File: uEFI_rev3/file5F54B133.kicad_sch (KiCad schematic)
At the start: 36 parts, among them U10 SensorsV2, U11 SensorsV2, U12 SensorsV2, U13 SensorsV2, U14 SensorsV2, U2 SensorsV2, U27 LM321, U31 LM321, U8 SensorsV2, U9 SensorsV2

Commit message: rev3, analog inputs
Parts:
- removed D14, D18: DZ2S033X0L, Diode_SMD:D_MiniMELF, symbol Diode:DZ2S033X0L
- removed JP11, JP19: Jumper_NC_Small, Jumper:SolderJumper-2_P1.3mm_Open_TrianglePad1.0x1.5mm, symbol Device:Jumper_NC_Small
- removed TP10, TP11, TP12, TP13, TP14, TP15, TP16, TP17: TestPoint, TestPoint:TestPoint_Pad_2.0x2.0mm, symbol Connector:TestPoint
- removed U10, U11, U12, U13, U14, U2, U8, U9: SensorsV2, OpenEFI-STM32F_rev3:Sensors_v2, symbol OpenEFI-STM32-rev3:SensorsV2
- added C1, C32, C35, C37, C38, C4: 240pF, Capacitor_SMD:C_0603_1608Metric, symbol Device:C_Small
- added C39: 100nF, Capacitor_SMD:C_0805_2012Metric, symbol Device:C_Small
- added C40: 4.7uF, Capacitor_SMD:C_0805_2012Metric, symbol Device:CP_Small
- added D15, D16, D17, D18, D19, D20, D21, D22, D23, D24, D25, D26, D27, D28, D29, D30: K26, Diode_SMD:D_SOD-123F, symbol Diode:PMEG2020EH
- added JP10, JP12, JP5, JP6, JP7, JP8, JP9: Jumper_NC_Small, Jumper:SolderJumper-2_P1.3mm_Open_TrianglePad1.0x1.5mm, symbol Device:Jumper_NC_Small
- added R36, R37, R42, R43, R49, R50: 28.6k +-1%, Resistor_SMD:R_0603_1608Metric, symbol Device:R_Small
- added R38, R39, R44, R45, R51, R52: 2.2k, Resistor_SMD:R_0603_1608Metric, symbol Device:R_Small
- added R40, R41, R47, R48, R53, R54: 3.32k +-1%, Resistor_SMD:R_0603_1608Metric, symbol Device:R_Small
- added R46: 0, Resistor_SMD:R_0603_1608Metric, symbol Device:R_Small
- added R55: 10k, Resistor_SMD:R_0603_1608Metric, symbol Device:R_Small
- added RV1: 2k, Potentiometer_THT:Potentiometer_Bourns_3386C_Horizontal, symbol Device:R_Potentiometer
- added U2: MCP3208, Package_SO:SOIC-16_3.9x9.9mm_P1.27mm, symbol Analog_ADC:MCP3208
- added U8: LM4040DBZ-5, Package_TO_SOT_SMD:SOT-23, symbol Reference_Voltage:LM4040DBZ-5
- added U9: AMS1117-5.0, Package_TO_SOT_SMD:SOT-223-3_TabPin2, symbol Regulator_Linear:AMS1117-5.0
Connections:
- net +12V: now also R55.2, U9.3 (VI)
- net B1: now also C1.1, R36.1, R38.2, R40.1; no longer C49.1, R87.1, R92.1, R97.2
- net C1: now also C4.1, R37.1, R39.2, R41.1
- net D1: now also C32.1, R42.1, R44.2, R47.1
- net E1: now also C35.1, R43.1, R45.2, R48.1
- net F1: now also C37.1, R49.1, R51.2, R53.1
- net G1: now also C38.1, R50.1, R52.2, R54.1
- net GND: now also R46.2, U2.9 (DGND); no longer C49.2, C51.2, R109.1, R83.2, R87.2, U27.2 (V-), U31.2 (V-)
- net K1: now also C49.1, R87.1, R92.1, R97.2
- net CH6: now reaches JP15.2, JP18.1, TP18.1, U31.4
- net CH6: now also D17.2 (A), D20.1 (K), U2.7 (CH6)
- net CH7: now reaches TP19.1, U27.3 (-), U27.4
- net CH7: now also D25.2 (A), D28.1 (K), JP12.1
- net +5V renamed +5C
- net +5C: now also C40.1, D15.1 (K), D16.1 (K), D17.1 (K), D21.1 (K), D22.1 (K), D25.1 (K), D26.1 (K), D27.1 (K), R36.2, R37.2, R42.2, R49.2, R50.2, U2.16 (Vdd), U9.2 (VO)
- new net: JP9.2, U2.5 (CH4)
- new net: C39.1, RV1.1, U9.1 (GND)
- new net: JP8.2, U2.4 (CH3)
- new net: JP10.2, U2.6 (CH5)
- new net: JP5.2, U2.1 (CH0)
- new net: JP6.2, U2.2 (CH1)
- new net: JP7.2, U2.3 (CH2)
- new net: JP12.2, U2.8 (CH7)
- new net +5VL: R55.1, U2.15 (Vref), U8.1 (K)
- new net ADC_CS: U2.10 (~{CS}/SHDN)
- new net CH0: D16.2 (A), D19.1 (K), JP5.1, R38.1
- new net CH1: D15.2 (A), D18.1 (K), JP6.1, R39.1
- new net CH2: D21.2 (A), D23.1 (K), JP7.1, R44.1
- new net CH3: D22.2 (A), D24.1 (K), JP8.1, R45.1
- new net CH4: D26.2 (A), D29.1 (K), JP9.1, R51.1
- new net CH5: D27.2 (A), D30.1 (K), JP10.1, R52.1
- new net GNDA: C1.2, C32.2, C35.2, C37.2, C38.2, C39.2, C4.2, C40.2, C49.2, C51.2, D18.2 (A), D19.2 (A), D20.2 (A), D23.2 (A), D24.2 (A), D28.2 (A), D29.2 (A), D30.2 (A), R109.1, R40.2, R41.2, R46.1, R47.2, R48.2, R53.2, R54.2, R83.2, R87.2, RV1.2, U2.14 (AGND), U27.2 (V-), U31.2 (V-), U8.2 (A)
- new net SPI2_MISO: U2.12 (Dout)
- new net SPI2_MOSI: U2.11 (Din)
- new net SPI2_SCK: U2.13 (CLK)
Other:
- note added: "0"
- note added: "1"
- note added: "2"
- note added: "3"
- note added: "4"
- note added: "5"
- note added: "5.5V"
- note added: "5v ADC Vref"
- note added: "5v ref: AnaSem VRH5501NTX LCSC C698020"
- note added: "ADC"
- note added: "AGND Star"
- note added: "Sensores: Temp Aire Temp Refrigerante TPS MAP O2 Bateria"
- note added: "Solo en puentear si no se utiliza una wideband"
- note removed: "AIR_TEMP"
- note removed: "PRES_FUEL"
- note removed: "PRES_OIL"
- note removed: "Solo en puentear si no te utiliza una wideband"
- note removed: "TEMP"
- note removed: "TPS"
- moved on the sheet: C49, C51, JP15, JP17, JP18, R108, R109, R82, R83, R87, R92, R97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

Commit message: rev3 ADC SPI
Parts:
- removed RV1: 2k, Potentiometer_THT:Potentiometer_Bourns_3386C_Horizontal, symbol Device:R_Potentiometer
- removed U9: AMS1117-5.0, Package_TO_SOT_SMD:SOT-223-3_TabPin2, symbol Regulator_Linear:AMS1117-5.0
- added R56: 750, Resistor_SMD:R_0603_1608Metric, symbol Device:R_Small
- added R57: 220, Resistor_SMD:R_0603_1608Metric, symbol Device:R_Small
- added U10, U11: TXS0102DCU, Package_SO:VSSOP-8_2.3x2mm_P0.5mm, symbol Logic_LevelTranslator:TXS0102DCU
- added U9: AMS1117, Package_TO_SOT_SMD:SOT-223-3_TabPin2, symbol Regulator_Linear:AMS1117
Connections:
- net +12V: now also U9.3 (VI)
- net +5C: now also R56.1, U9.2 (VO)
- net ADC_CS: now also U11.4 (A2); no longer U2.10 (~{CS}/SHDN)
- net GND: now also U10.2 (GND), U11.2 (GND)
- net GNDA: now also R57.1
- net SPI2_MISO: now also U10.4 (A2); no longer U2.12 (Dout)
- net SPI2_MOSI: now also U11.5 (A1); no longer U2.11 (Din)
- net SPI2_SCK: now also U10.5 (A1); no longer U2.13 (CLK)
- net at C39.1: now also R56.2, R57.2, U9.1 (ADJ)
- new net +3V3: U10.3 (VCCA), U10.6 (OE), U11.3 (VCCA), U11.6 (OE)
- new net +5V: U10.7 (VCCB), U11.7 (VCCB)
- new net CLK: U10.8 (B1), U2.13 (CLK)
- new net CS: U11.1 (B2), U2.10 (~{CS}/SHDN)
- new net DIN: U11.8 (B1), U2.11 (Din)
- new net DOUT: U10.1 (B2), U2.12 (Dout)
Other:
- note added: "SPI 5V => 3V"

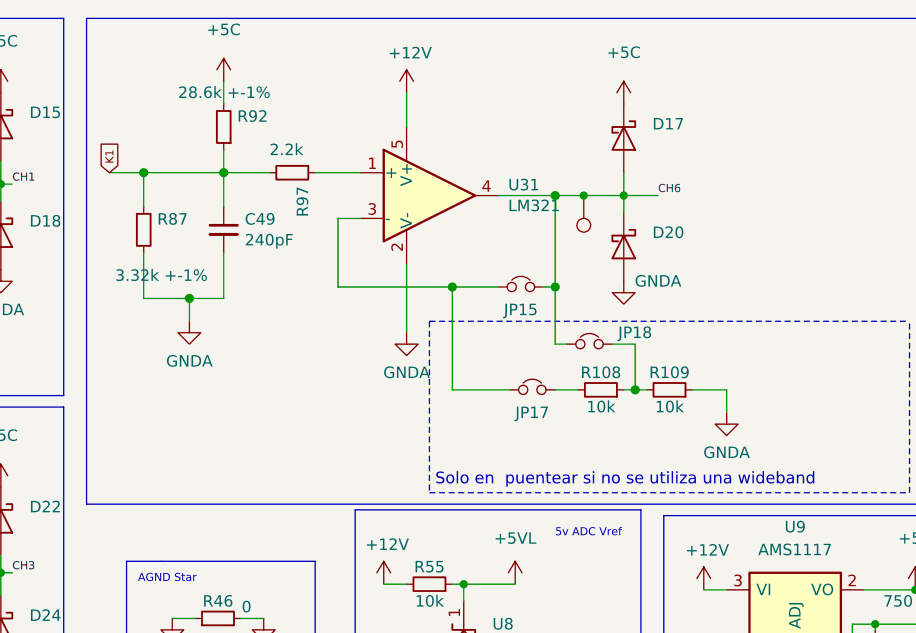
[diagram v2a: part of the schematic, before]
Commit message: rev3, PMIC, Relays done
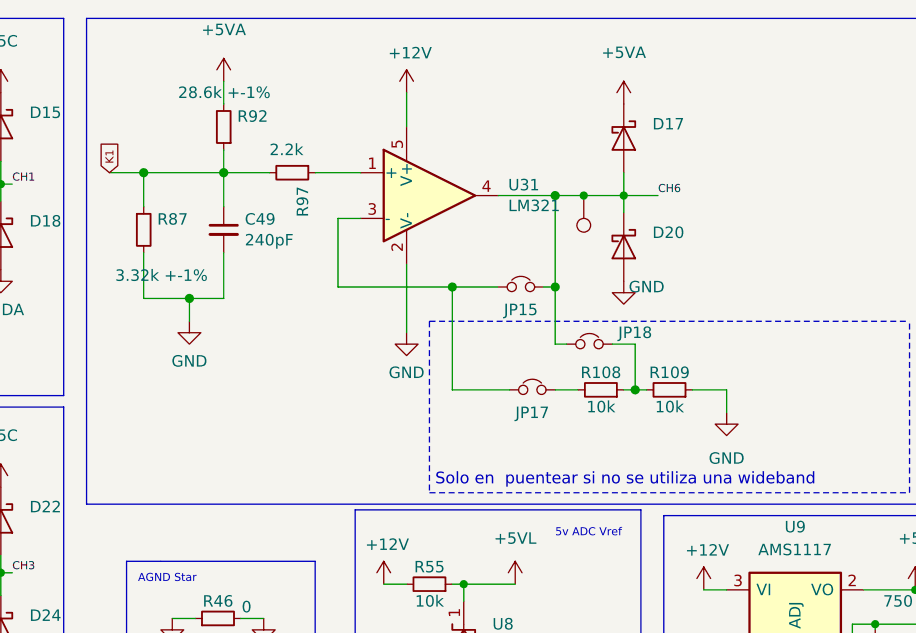
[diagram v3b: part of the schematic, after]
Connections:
- net +5C: no longer D17.1 (K), R92.2
- net GND: now also C49.2, D20.2 (A), R109.1, R87.2, U31.2 (V-)
- net GNDA: no longer C49.2, D20.2 (A), R109.1, R87.2, U31.2 (V-)
- new net +5VA: D17.1 (K), R92.2
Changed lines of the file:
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@@
   (symbol (lib_id "power:+5V") (at 283.21 222.25 0) (unit 1)
     (in_bom yes) (on_board yes) (fields_autoplaced)
-    (property "Reference" "#PWR?" (id 0) (at 283.21 226.06 0)
+    (property "Reference" "#PWR0138" (id 0) (at 283.21 226.06 0)
       (effects (font (size 1.27 1.27)) hide)
     )
@@
     (pin "2")
   )
+  (symbol (lib_id "power:GND") (at 176.53 118.11 0) (unit 1)
+    (in_bom yes) (on_board yes)
+    (property "Reference" "#PWR?" (id 0) (at 176.53 124.46 0)
+      (effects (font (size 1.27 1.27)) hide)
+    )
+    (property "Value" "GND" (id 1) (at 176.53 122.555 0))
+    (property "Footprint" "" (id 2) (at 176.53 118.11 0)
+      (effects (font (size 1.27 1.27)) hide)
+    )
+    (property "Datasheet" "" (id 3) (at 176.53 118.11 0)
+      (effects (font (size 1.27 1.27)) hide)
+    )
+    (pin "1")
+  )
   (symbol (lib_id "Diode:PMEG2020EH") (at 224.79 109.855 270) (unit 1)
     (in_bom yes) (on_board yes) (fields_autoplaced)
@@
     (pin "1")
     (pin "2")
-  )
-  (symbol (lib_id "power:+5C") (at 224.79 93.98 0) (unit 1)
-    (in_bom yes) (on_board yes) (fields_autoplaced)
-    (property "Reference" "#PWR076" (id 0) (at 224.79 97.79 0)
-      (effects (font (size 1.27 1.27)) hide)
-    )
-    (property "Value" "+5C" (id 1) (at 224.79 88.265 0))
-    (property "Footprint" "" (id 2) (at 224.79 93.98 0)
-      (effects (font (size 1.27 1.27)) hide)
-    )
-    (property "Datasheet" "" (id 3) (at 224.79 93.98 0)
-      (effects (font (size 1.27 1.27)) hide)
-    )
-    (pin "1")
   )
   (symbol (lib_id "Device:Jumper_NC_Small") (at 241.3 186.055 0) (unit 1)
@@
     (pin "2")
   )
-  (symbol (lib_id "power:+5C") (at 180.34 91.44 0) (unit 1)
-    (in_bom yes) (on_board yes) (fields_autoplaced)
-    (property "Reference" "#PWR070" (id 0) (at 180.34 95.25 0)
-      (effects (font (size 1.27 1.27)) hide)
-    )
-    (property "Value" "+5C" (id 1) (at 180.34 85.725 0))
-    (property "Footprint" "" (id 2) (at 180.34 91.44 0)
-      (effects (font (size 1.27 1.27)) hide)
-    )
-    (property "Datasheet" "" (id 3) (at 180.34 91.44 0)
-      (effects (font (size 1.27 1.27)) hide)
-    )
-    (pin "1")
-  )
   (symbol (lib_id "Device:Jumper_NC_Small") (at 241.3 191.135 0) (unit 1)
     (in_bom yes) (on_board yes)
@@
     )
     (property "Datasheet" "" (id 3) (at 267.335 201.295 0)
-      (effects (font (size 1.27 1.27)) hide)
-    )
-    (pin "1")
-  )
-  (symbol (lib_id "power:GNDA") (at 176.53 118.11 0) (unit 1)
-    (in_bom yes) (on_board yes) (fields_autoplaced)
-    (property "Reference" "#PWR055" (id 0) (at 176.53 124.46 0)
-      (effects (font (size 1.27 1.27)) hide)
-    )
-    (property "Value" "GNDA" (id 1) (at 176.53 122.555 0))
-    (property "Footprint" "" (id 2) (at 176.53 118.11 0)
-      (effects (font (size 1.27 1.27)) hide)
-    )
-    (property "Datasheet" "" (id 3) (at 176.53 118.11 0)
       (effects (font (size 1.27 1.27)) hide)
     )
@@
     (pin "1")
   )
+  (symbol (lib_id "power:GND") (at 200.66 119.38 0) (unit 1)
+    (in_bom yes) (on_board yes)
+    (property "Reference" "#PWR?" (id 0) (at 200.66 125.73 0)
+      (effects (font (size 1.27 1.27)) hide)
+    )
+    (property "Value" "GND" (id 1) (at 200.66 123.825 0))
+    (property "Footprint" "" (id 2) (at 200.66 119.38 0)
+      (effects (font (size 1.27 1.27)) hide)
+    )
+    (property "Datasheet" "" (id 3) (at 200.66 119.38 0)
+      (effects (font (size 1.27 1.27)) hide)
+    )
+    (pin "1")
+  )
   (symbol (lib_id "power:+5C") (at 144.145 179.07 0) (unit 1)
     (in_bom yes) (on_board yes) (fields_autoplaced)
@@
     )
     (property "Datasheet" "" (id 3) (at 233.68 147.955 0)
-      (effects (font (size 1.27 1.27)) hide)
-    )
-    (pin "1")
-  )
-  (symbol (lib_id "power:GNDA") (at 224.79 113.665 0) (unit 1)
-    (in_bom yes) (on_board yes)
-    (property "Reference" "#PWR043" (id 0) (at 224.79 120.015 0)
-      (effects (font (size 1.27 1.27)) hide)
-    )
-    (property "Value" "GNDA" (id 1) (at 228.6 113.665 0))
-    (property "Footprint" "" (id 2) (at 224.79 113.665 0)
-      (effects (font (size 1.27 1.27)) hide)
-    )
-    (property "Datasheet" "" (id 3) (at 224.79 113.665 0)
       (effects (font (size 1.27 1.27)) hide)
     )
@@
     (pin "1")
   )
-  (symbol (lib_id "power:GNDA") (at 200.66 119.38 0) (unit 1)
-    (in_bom yes) (on_board yes) (fields_autoplaced)
-    (property "Reference" "#PWR058" (id 0) (at 200.66 125.73 0)
-      (effects (font (size 1.27 1.27)) hide)
-    )
-    (property "Value" "GNDA" (id 1) (at 200.66 123.825 0))
-    (property "Footprint" "" (id 2) (at 200.66 119.38 0)
-      (effects (font (size 1.27 1.27)) hide)
-    )
-    (property "Datasheet" "" (id 3) (at 200.66 119.38 0)
-      (effects (font (size 1.27 1.27)) hide)
-    )
-    (pin "1")
-  )
   (symbol (lib_id "power:+5C") (at 113.03 93.98 0) (unit 1)
     (in_bom yes) (on_board yes) (fields_autoplaced)
@@
     )
     (property "Datasheet" "" (id 3) (at 99.06 162.56 0)
-      (effects (font (size 1.27 1.27)) hide)
-    )
-    (pin "1")
-  )
-  (symbol (lib_id "power:GNDA") (at 236.22 128.27 0) (unit 1)
-    (in_bom yes) (on_board yes) (fields_autoplaced)
-    (property "Reference" "#PWR059" (id 0) (at 236.22 134.62 0)
-      (effects (font (size 1.27 1.27)) hide)
-    )
-    (property "Value" "GNDA" (id 1) (at 236.22 132.715 0))
-    (property "Footprint" "" (id 2) (at 236.22 128.27 0)
-      (effects (font (size 1.27 1.27)) hide)
-    )
-    (property "Datasheet" "" (id 3) (at 236.22 128.27 0)
       (effects (font (size 1.27 1.27)) hide)
     )
@@
     (pin "2")
   )
+  (symbol (lib_id "power:GND") (at 236.22 128.27 0) (unit 1)
+    (in_bom yes) (on_board yes) (fields_autoplaced)
+    (property "Reference" "#PWR?" (id 0) (at 236.22 134.62 0)
+      (effects (font (size 1.27 1.27)) hide)
+    )
+    (property "Value" "GND" (id 1) (at 236.22 133.35 0))
+    (property "Footprint" "" (id 2) (at 236.22 128.27 0)
+      (effects (font (size 1.27 1.27)) hide)
+    )
+    (property "Datasheet" "" (id 3) (at 236.22 128.27 0)
+      (effects (font (size 1.27 1.27)) hide)
+    )
+    (pin "1")
+  )
+  (symbol (lib_id "power:+5VA") (at 180.34 91.44 0) (unit 1)
+    (in_bom yes) (on_board yes) (fields_autoplaced)
+    (property "Reference" "#PWR0154" (id 0) (at 180.34 95.25 0)
+      (effects (font (size 1.27 1.27)) hide)
+    )
+    (property "Value" "+5VA" (id 1) (at 180.34 85.725 0))
+    (property "Footprint" "" (id 2) (at 180.34 91.44 0)
+      (effects (font (size 1.27 1.27)) hide)
+    )
+    (property "Datasheet" "" (id 3) (at 180.34 91.44 0)
+      (effects (font (size 1.27 1.27)) hide)
+    )
+    (pin "1")
+  )
   (symbol (lib_id "Device:R_Small") (at 151.765 189.23 270) (unit 1)
     (in_bom yes) (on_board yes)
@@
     )
     (property "Datasheet" "" (id 3) (at 155.575 112.395 0)
+      (effects (font (size 1.27 1.27)) hide)
+    )
+    (pin "1")
+  )
+  (symbol (lib_id "power:+5VA") (at 224.79 93.98 0) (unit 1)
+    (in_bom yes) (on_board yes) (fields_autoplaced)
+    (property "Reference" "#PWR0155" (id 0) (at 224.79 97.79 0)
+      (effects (font (size 1.27 1.27)) hide)
+    )
+    (property "Value" "+5VA" (id 1) (at 224.79 88.265 0))
+    (property "Footprint" "" (id 2) (at 224.79 93.98 0)
+      (effects (font (size 1.27 1.27)) hide)
+    )
+    (property "Datasheet" "" (id 3) (at 224.79 93.98 0)
       (effects (font (size 1.27 1.27)) hide)
     )
@@
       (effects (font (size 1.27 1.27)) hide)
     )
+    (pin "1")
+  )
+  (symbol (lib_id "power:GND") (at 224.79 113.665 0) (unit 1)
+    (in_bom yes) (on_board yes)
+    (property "Reference" "#PWR?" (id 0) (at 224.79 120.015 0)
+      (effects (font (size 1.27 1.27)) hide)
+    )
+    (property "Value" "GND" (id 1) (at 227.33 114.3 0))
+    (property "Footprint" "" (id 2) (at 224.79 113.665 0)
+      (effects (font (size 1.27 1.27)) hide)
+    )
+    (property "Datasheet" "" (id 3) (at 224.79 113.665 0)
+      (effects (font (size 1.27 1.27)) hide)
+    )

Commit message: uEFI rev 3.1.0
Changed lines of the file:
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@@
     (stroke (width 0) (type dash) (color 0 0 0 0))
   )
-  (polyline (pts (xy 123.825 84.455) (xy 162.56 84.455))
+  (polyline (pts (xy 123.825 84.455) (xy 163.83 84.455))
     (stroke (width 0) (type default) (color 0 0 0 0))
   )
@@
     (stroke (width 0) (type default) (color 0 0 0 0))
   )
-  (polyline (pts (xy 121.285 127.635) (xy 121.285 169.545))
+  (polyline (pts (xy 121.92 127.635) (xy 121.92 169.545))
     (stroke (width 0) (type default) (color 0 0 0 0))
   )
@@
     (stroke (width 0) (type solid) (color 0 0 0 0))
   )
-  (polyline (pts (xy 121.285 169.545) (xy 82.55 169.545))
+  (polyline (pts (xy 121.92 169.545) (xy 82.55 169.545))
     (stroke (width 0) (type default) (color 0 0 0 0))
   )
@@
     (stroke (width 0) (type default) (color 0 0 0 0))
   )
-  (polyline (pts (xy 162.56 84.455) (xy 162.56 126.365))
+  (polyline (pts (xy 163.83 84.455) (xy 163.83 126.365))
     (stroke (width 0) (type default) (color 0 0 0 0))
   )
@@
     (stroke (width 0) (type solid) (color 0 0 0 0))
   )
-  (polyline (pts (xy 82.55 127.635) (xy 121.285 127.635))
+  (polyline (pts (xy 82.55 127.635) (xy 121.92 127.635))
     (stroke (width 0) (type default) (color 0 0 0 0))
   )
@@
     (stroke (width 0) (type default) (color 0 0 0 0))
   )
-  (polyline (pts (xy 162.56 126.365) (xy 123.825 126.365))
-    (stroke (width 0) (type default) (color 0 0 0 0))
-  )
+  (polyline (pts (xy 163.83 126.365) (xy 123.825 126.365))
+    (stroke (width 0) (type default) (color 0 0 0 0))
+  )

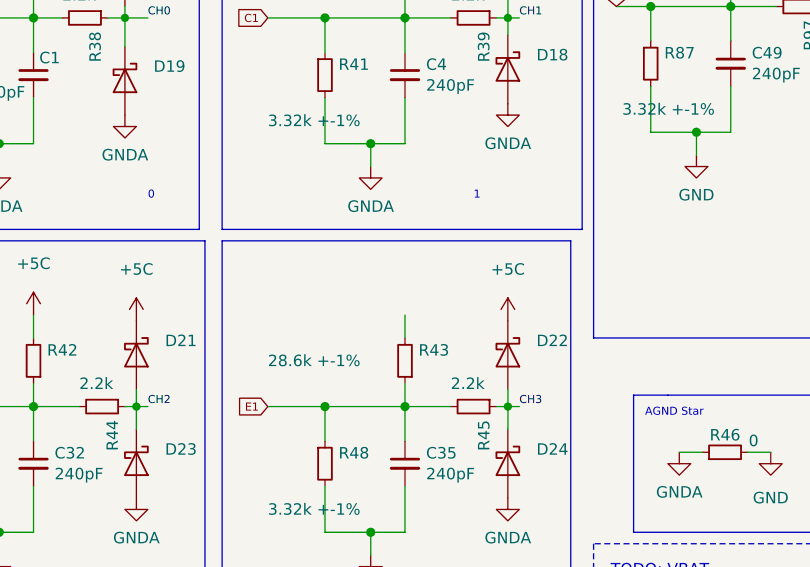
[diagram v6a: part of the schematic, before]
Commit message: add ckp sensor setup
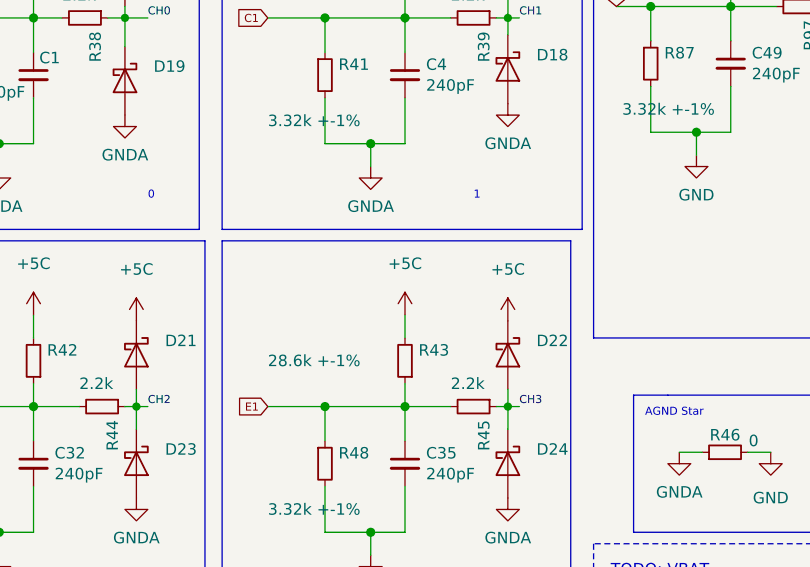
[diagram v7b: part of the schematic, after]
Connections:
- net +5C: now also R43.2
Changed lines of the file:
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@@
     (stroke (width 0) (type solid) (color 0 0 0 0))
-  )
-  (wire (pts (xy 235.585 193.675) (xy 247.015 193.675))
-    (stroke (width 0) (type default) (color 0 0 0 0))
   )
   (wire (pts (xy 257.175 147.955) (xy 265.43 147.955))
@@
   (polyline (pts (xy 290.83 161.29) (xy 229.235 161.29))
     (stroke (width 0) (type dash) (color 0 0 0 0))
+  )
+  (wire (pts (xy 235.585 193.675) (xy 247.015 193.675))
+    (stroke (width 0) (type default) (color 0 0 0 0))
   )
   (wire (pts (xy 114.3 146.05) (xy 114.3 148.59))
@@
     (pin "2")
   )
+  (symbol (lib_id "power:+5C") (at 144.145 135.89 0) (unit 1)
+    (in_bom yes) (on_board yes) (fields_autoplaced)
+    (property "Reference" "#PWR043" (id 0) (at 144.145 139.7 0)
+      (effects (font (size 1.27 1.27)) hide)
+    )
+    (property "Value" "+5C" (id 1) (at 144.145 130.175 0))
+    (property "Footprint" "" (id 2) (at 144.145 135.89 0)
+      (effects (font (size 1.27 1.27)) hide)
+    )
+    (property "Datasheet" "" (id 3) (at 144.145 135.89 0)
+      (effects (font (size 1.27 1.27)) hide)
+    )
+    (pin "1")
+  )
   (symbol (lib_id "power:GNDA") (at 99.06 119.38 0) (unit 1)
